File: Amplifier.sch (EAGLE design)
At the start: 34 parts, among them IC1 OP213, J1 ARDUINO_R3_SHIELD

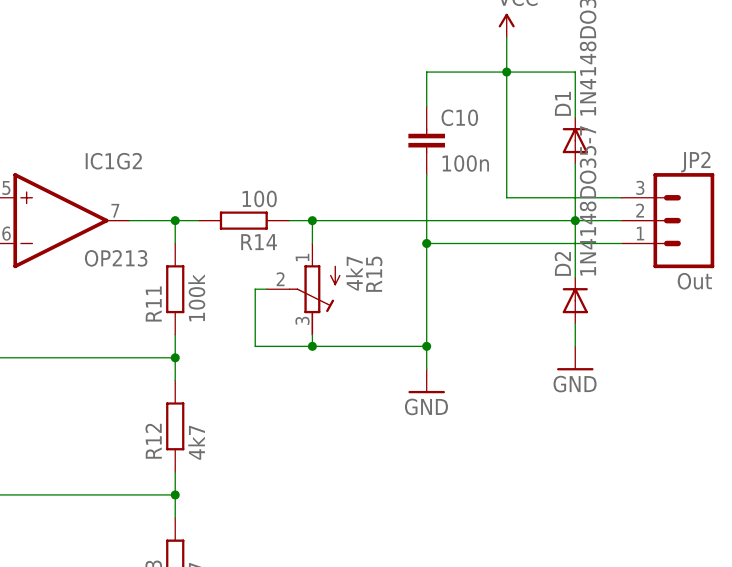
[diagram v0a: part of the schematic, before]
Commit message: Stupid bug in output stage fixed
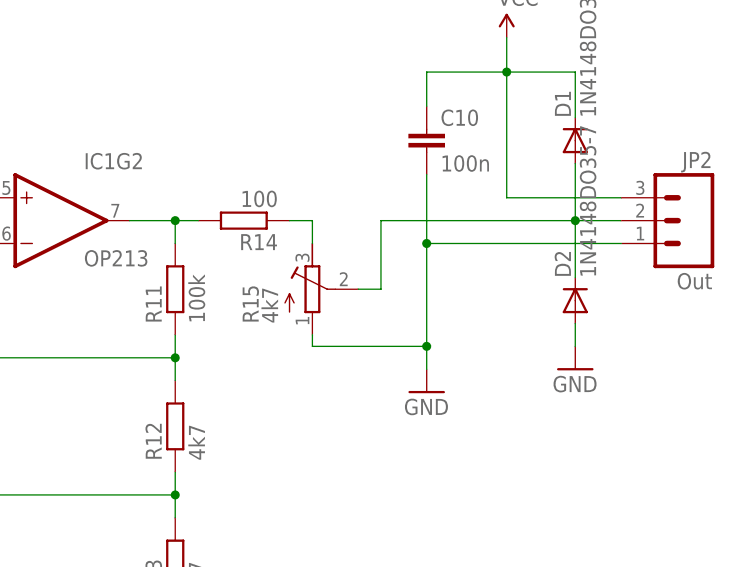
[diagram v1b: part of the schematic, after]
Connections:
- new net N$18: R14.1, R15.E
- net GEOPHONE_OUT: now also R15.S; no longer R14.1, R15.A
- net GND: now also R15.A; no longer R15.E, R15.S
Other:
- moved on the sheet: R15
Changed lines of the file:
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@@
 <instance part="C10" gate="G$1" x="238.76" y="66.04"/>
 <instance part="SUPPLY3" gate="G$1" x="247.65" y="76.2"/>
-<instance part="R15" gate="G$1" x="226.06" y="48.26" rot="R180"/>
+<instance part="R15" gate="G$1" x="226.06" y="48.26"/>
 <instance part="J1" gate="G$1" x="172.72" y="106.68"/>
 <instance part="SUPPLY4" gate="G$1" x="138.43" y="119.38"/>
@@
 <junction x="238.76" y="53.34"/>
 <junction x="238.76" y="41.91"/>
-<pinref part="R15" gate="G$1" pin="E"/>
 <wire x1="238.76" y1="41.91" x2="226.06" y2="41.91" width="0.1524" layer="91"/>
+<pinref part="GND8" gate="1" pin="GND"/>
+<pinref part="R15" gate="G$1" pin="A"/>
 <wire x1="226.06" y1="41.91" x2="226.06" y2="43.18" width="0.1524" layer="91"/>
-<pinref part="R15" gate="G$1" pin="S"/>
-<wire x1="220.98" y1="48.26" x2="219.71" y2="48.26" width="0.1524" layer="91"/>
-<wire x1="219.71" y1="48.26" x2="219.71" y2="41.91" width="0.1524" layer="91"/>
-<wire x1="219.71" y1="41.91" x2="226.06" y2="41.91" width="0.1524" layer="91"/>
-<junction x="226.06" y="41.91"/>
-<pinref part="GND8" gate="1" pin="GND"/>
 </segment>
 <segment>
@@
 <net name="GEOPHONE_OUT" class="0">
 <segment>
-<pinref part="R14" gate="G$1" pin="1"/>
-<wire x1="223.52" y1="55.88" x2="226.06" y2="55.88" width="0.1524" layer="91"/>
 <pinref part="JP2" gate="G$1" pin="2"/>
-<wire x1="226.06" y1="55.88" x2="255.27" y2="55.88" width="0.1524" layer="91"/>
-<pinref part="R15" gate="G$1" pin="A"/>
 <wire x1="255.27" y1="55.88" x2="260.35" y2="55.88" width="0.1524" layer="91"/>
-<wire x1="226.06" y1="53.34" x2="226.06" y2="55.88" width="0.1524" layer="91"/>
-<junction x="226.06" y="55.88"/>
 <pinref part="D1" gate="G$1" pin="A"/>
 <wire x1="255.27" y1="62.23" x2="255.27" y2="55.88" width="0.1524" layer="91"/>
@@
 <pinref part="D2" gate="G$1" pin="C"/>
 <wire x1="255.27" y1="55.88" x2="255.27" y2="49.53" width="0.1524" layer="91"/>
+<wire x1="233.68" y1="48.26" x2="233.68" y2="55.88" width="0.1524" layer="91"/>
+<wire x1="233.68" y1="55.88" x2="255.27" y2="55.88" width="0.1524" layer="91"/>
+<pinref part="R15" gate="G$1" pin="S"/>
+<wire x1="231.14" y1="48.26" x2="233.68" y2="48.26" width="0.1524" layer="91"/>
 </segment>
 <segment>
@@
 </segment>
 </net>
+<net name="N$18" class="0">
+<segment>
+<pinref part="R14" gate="G$1" pin="1"/>
+<wire x1="223.52" y1="55.88" x2="226.06" y2="55.88" width="0.1524" layer="91"/>
+<pinref part="R15" gate="G$1" pin="E"/>
+<wire x1="226.06" y1="55.88" x2="226.06" y2="53.34" width="0.1524" layer="91"/>
+</segment>
+</net>

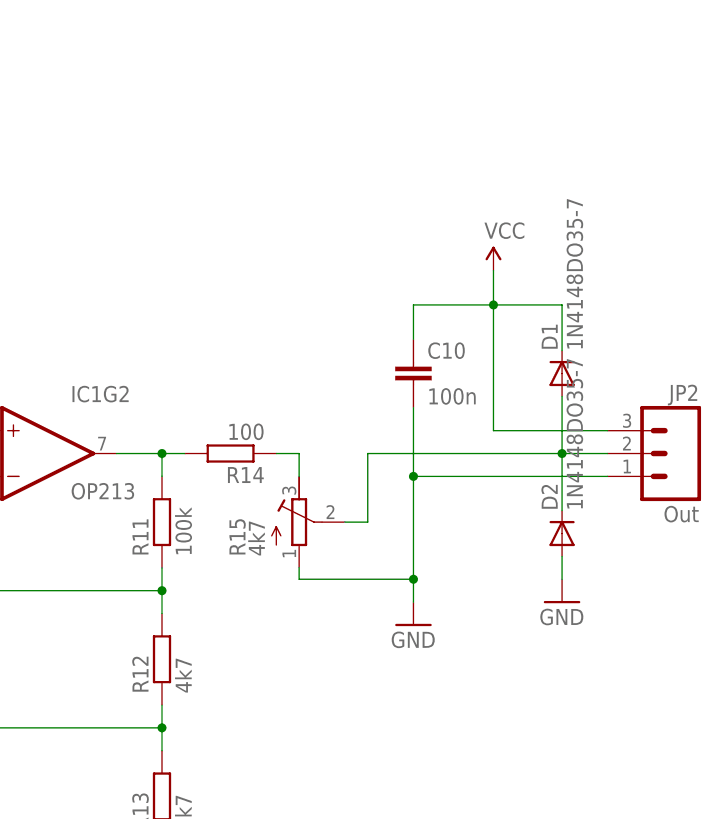
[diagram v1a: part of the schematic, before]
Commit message: Bug in output stage fixed, redundant capacitor removed.
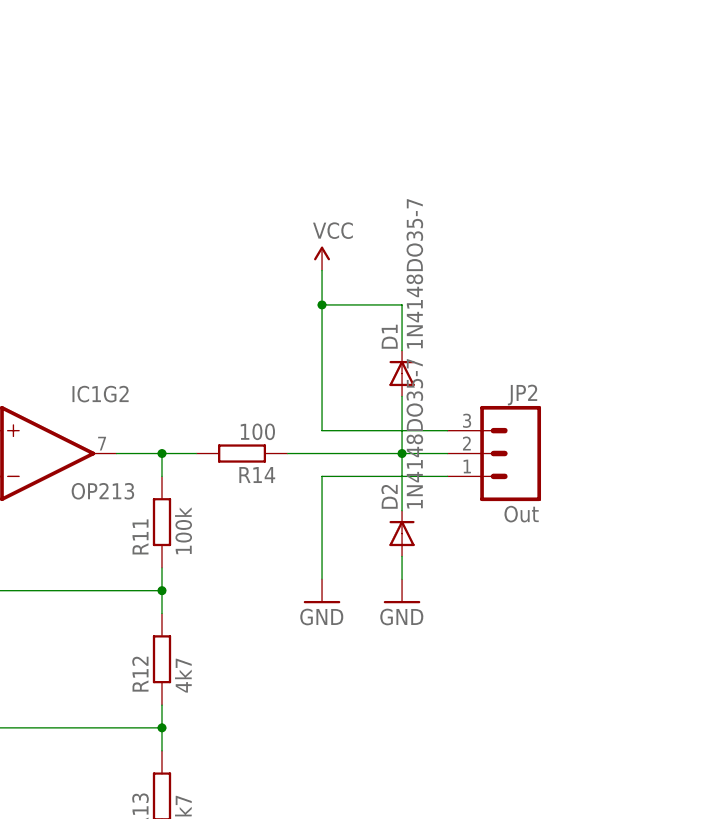
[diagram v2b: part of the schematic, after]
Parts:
- removed C10: 100n, rcl:C-EU025-025X050
- removed R15: 4k7, rcl:R-TRIMM64Y
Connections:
- removed net N$18: R14.1, R15.E
- net GEOPHONE_OUT: now also R14.1; no longer R15.S
- net GND: no longer C10.2, R15.A
- net VCC: no longer C10.1
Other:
- moved on the sheet: D1, D2, JP2, R14
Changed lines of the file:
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@@
 <setting verticaltext="up"/>
 </settings>
-<grid distance="0.05" unitdist="inch" unit="inch" style="lines" multiple="1" display="yes" altdistance="0.01" altunitdist="inch" altunit="inch"/>
+<grid distance="0.05" unitdist="inch" unit="inch" style="lines" multiple="1" display="no" altdistance="0.01" altunitdist="inch" altunit="inch"/>
 <layers>
 <layer number="1" name="Top" color="4" fill="1" visible="no" active="no"/>
@@
 <part name="R14" library="resistor" deviceset="R-EU_" device="0207/12" value="100"/>
 <part name="JP2" library="SparkFun-Connectors" deviceset="M03" device="LONGPADS" value="Out"/>
-<part name="C10" library="rcl" deviceset="C-EU" device="025-025X050" value="100n"/>
 <part name="SUPPLY3" library="SparkFun-Aesthetics" deviceset="VCC" device="" value="VCC"/>
-<part name="R15" library="rcl" deviceset="R-TRIMM" device="64Y" value="4k7"/>
 <part name="J1" library="SparkFun-Boards" deviceset="ARDUINO_R3_SHIELD" device=""/>
 <part name="SUPPLY4" library="SparkFun-Aesthetics" deviceset="VCC" device="" value="VCC"/>
@@
 <instance part="R13" gate="G$1" x="210.82" y="17.78" rot="R90"/>
 <instance part="C9" gate="G$1" x="210.82" y="7.62"/>
-<instance part="R14" gate="G$1" x="218.44" y="55.88" rot="R180"/>
-<instance part="JP2" gate="G$1" x="267.97" y="55.88" rot="MR0"/>
-<instance part="C10" gate="G$1" x="238.76" y="66.04"/>
-<instance part="SUPPLY3" gate="G$1" x="247.65" y="76.2"/>
-<instance part="R15" gate="G$1" x="226.06" y="48.26"/>
+<instance part="R14" gate="G$1" x="219.71" y="55.88" rot="R180"/>
+<instance part="JP2" gate="G$1" x="250.19" y="55.88" rot="MR0"/>
+<instance part="SUPPLY3" gate="G$1" x="228.6" y="76.2"/>
 <instance part="J1" gate="G$1" x="172.72" y="106.68"/>
 <instance part="SUPPLY4" gate="G$1" x="138.43" y="119.38"/>
@@
 <instance part="GND6" gate="1" x="210.82" y="-2.54"/>
 <instance part="GND7" gate="1" x="151.13" y="78.74"/>
-<instance part="GND8" gate="1" x="238.76" y="36.83"/>
-<instance part="D1" gate="G$1" x="255.27" y="64.77" rot="R90"/>
-<instance part="D2" gate="G$1" x="255.27" y="46.99" rot="R90"/>
-<instance part="GND9" gate="1" x="255.27" y="39.37"/>
+<instance part="GND8" gate="1" x="228.6" y="39.37"/>
+<instance part="D1" gate="G$1" x="237.49" y="64.77" rot="R90"/>
+<instance part="D2" gate="G$1" x="237.49" y="46.99" rot="R90"/>
+<instance part="GND9" gate="1" x="237.49" y="39.37"/>
 <instance part="JP3" gate="A" x="127" y="93.98" rot="R180"/>
 <instance part="L1" gate="G$1" x="138.43" y="109.22"/>
@@
 <segment>
 <pinref part="JP2" gate="G$1" pin="3"/>
-<wire x1="260.35" y1="58.42" x2="247.65" y2="58.42" width="0.1524" layer="91"/>
-<wire x1="247.65" y1="58.42" x2="247.65" y2="72.39" width="0.1524" layer="91"/>
-<wire x1="247.65" y1="72.39" x2="238.76" y2="72.39" width="0.1524" layer="91"/>
-<wire x1="238.76" y1="72.39" x2="238.76" y2="68.58" width="0.1524" layer="91"/>
-<pinref part="C10" gate="G$1" pin="1"/>
-<wire x1="247.65" y1="72.39" x2="247.65" y2="76.2" width="0.1524" layer="91"/>
-<junction x="247.65" y="72.39"/>
+<wire x1="242.57" y1="58.42" x2="228.6" y2="58.42" width="0.1524" layer="91"/>
+<wire x1="228.6" y1="58.42" x2="228.6" y2="72.39" width="0.1524" layer="91"/>
+<wire x1="228.6" y1="72.39" x2="228.6" y2="76.2" width="0.1524" layer="91"/>
+<junction x="228.6" y="72.39"/>
 <pinref part="SUPPLY3" gate="G$1" pin="VCC"/>
 <pinref part="D1" gate="G$1" pin="C"/>
-<wire x1="247.65" y1="72.39" x2="255.27" y2="72.39" width="0.1524" layer="91"/>
-<wire x1="255.27" y1="72.39" x2="255.27" y2="67.31" width="0.1524" layer="91"/>
+<wire x1="228.6" y1="72.39" x2="237.49" y2="72.39" width="0.1524" layer="91"/>
+<wire x1="237.49" y1="72.39" x2="237.49" y2="67.31" width="0.1524" layer="91"/>
 </segment>
 <segment>
@@
 <pinref part="R11" gate="G$1" pin="2"/>
 <pinref part="R14" gate="G$1" pin="2"/>
-<wire x1="213.36" y1="55.88" x2="210.82" y2="55.88" width="0.1524" layer="91"/>
+<wire x1="214.63" y1="55.88" x2="210.82" y2="55.88" width="0.1524" layer="91"/>
 <junction x="210.82" y="55.88"/>
 </segment>
@@
 </segment>
 <segment>
-<wire x1="260.35" y1="53.34" x2="238.76" y2="53.34" width="0.1524" layer="91"/>
-<wire x1="238.76" y1="53.34" x2="238.76" y2="41.91" width="0.1524" layer="91"/>
+<wire x1="242.57" y1="53.34" x2="228.6" y2="53.34" width="0.1524" layer="91"/>
+<wire x1="228.6" y1="53.34" x2="228.6" y2="41.91" width="0.1524" layer="91"/>
 <pinref part="JP2" gate="G$1" pin="1"/>
-<pinref part="C10" gate="G$1" pin="2"/>
-<wire x1="238.76" y1="41.91" x2="238.76" y2="39.37" width="0.1524" layer="91"/>
-<wire x1="238.76" y1="60.96" x2="238.76" y2="53.34" width="0.1524" layer="91"/>
-<junction x="238.76" y="53.34"/>
-<junction x="238.76" y="41.91"/>
-<wire x1="238.76" y1="41.91" x2="226.06" y2="41.91" width="0.1524" layer="91"/>
 <pinref part="GND8" gate="1" pin="GND"/>
-<pinref part="R15" gate="G$1" pin="A"/>
-<wire x1="226.06" y1="41.91" x2="226.06" y2="43.18" width="0.1524" layer="91"/>
 </segment>
 <segment>
@@
 <segment>
 <pinref part="D2" gate="G$1" pin="A"/>
-<wire x1="255.27" y1="44.45" x2="255.27" y2="41.91" width="0.1524" layer="91"/>
+<wire x1="237.49" y1="44.45" x2="237.49" y2="41.91" width="0.1524" layer="91"/>
 <pinref part="GND9" gate="1" pin="GND"/>
 </segment>
@@
 <segment>
 <pinref part="JP2" gate="G$1" pin="2"/>
-<wire x1="255.27" y1="55.88" x2="260.35" y2="55.88" width="0.1524" layer="91"/>
+<wire x1="237.49" y1="55.88" x2="242.57" y2="55.88" width="0.1524" layer="91"/>
 <pinref part="D1" gate="G$1" pin="A"/>
-<wire x1="255.27" y1="62.23" x2="255.27" y2="55.88" width="0.1524" layer="91"/>
-<junction x="255.27" y="55.88"/>
+<wire x1="237.49" y1="62.23" x2="237.49" y2="55.88" width="0.1524" layer="91"/>
+<junction x="237.49" y="55.88"/>
 <pinref part="D2" gate="G$1" pin="C"/>
-<wire x1="255.27" y1="55.88" x2="255.27" y2="49.53" width="0.1524" layer="91"/>
-<wire x1="233.68" y1="48.26" x2="233.68" y2="55.88" width="0.1524" layer="91"/>
-<wire x1="233.68" y1="55.88" x2="255.27" y2="55.88" width="0.1524" layer="91"/>
-<pinref part="R15" gate="G$1" pin="S"/>
-<wire x1="231.14" y1="48.26" x2="233.68" y2="48.26" width="0.1524" layer="91"/>
+<wire x1="237.49" y1="55.88" x2="237.49" y2="49.53" width="0.1524" layer="91"/>
+<wire x1="224.79" y1="55.88" x2="237.49" y2="55.88" width="0.1524" layer="91"/>
+<pinref part="R14" gate="G$1" pin="1"/>
 </segment>
 <segment>
@@
 </segment>
 </net>
-<net name="N$18" class="0">
-<segment>
-<pinref part="R14" gate="G$1" pin="1"/>
-<wire x1="223.52" y1="55.88" x2="226.06" y2="55.88" width="0.1524" layer="91"/>
-<pinref part="R15" gate="G$1" pin="E"/>
-<wire x1="226.06" y1="55.88" x2="226.06" y2="53.34" width="0.1524" layer="91"/>
-</segment>
-</net>
